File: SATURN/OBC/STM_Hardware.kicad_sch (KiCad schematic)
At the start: 6 parts, among them J1 SWD Pins, J2 USB_OTG, U1 USBLC6-4SC6

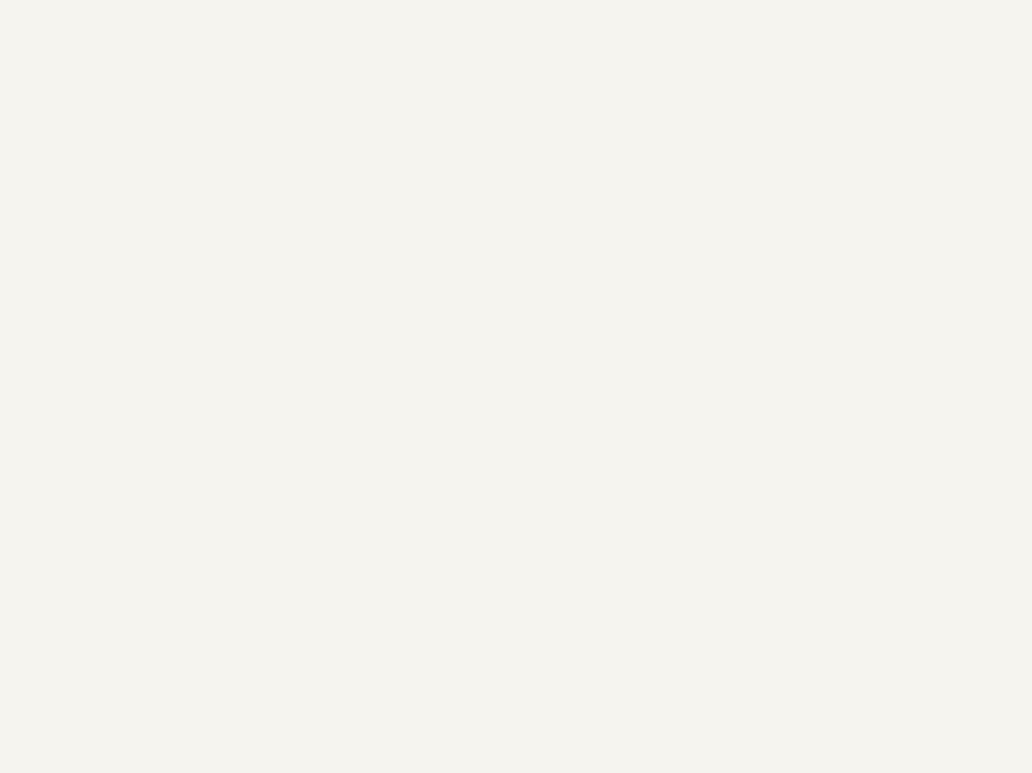
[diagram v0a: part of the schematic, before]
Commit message: Wired Up Watchdogs. Hopefully correctly.
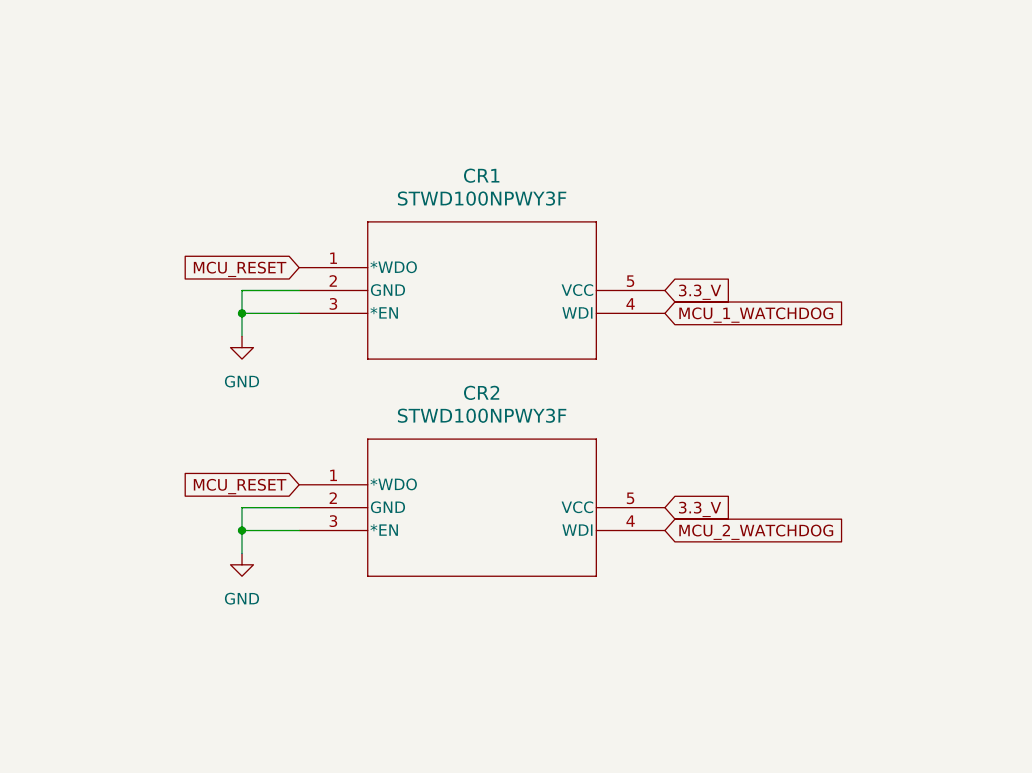
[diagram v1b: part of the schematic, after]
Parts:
- added CR1, CR2: STWD100NPWY3F, SOT23-5L_STM, symbol OBC-Components:STWD100NPWY3F
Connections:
- net GND: now also CR1.2 (GND), CR1.3 (*EN), CR2.2 (GND), CR2.3 (*EN)
- new net 3.3_V: CR1.5 (VCC), CR2.5 (VCC)
- new net MCU_1_WATCHDOG: CR1.4 (WDI)
- new net MCU_2_WATCHDOG: CR2.4 (WDI)
- new net MCU_RESET: CR1.1 (*WDO), CR2.1 (*WDO)

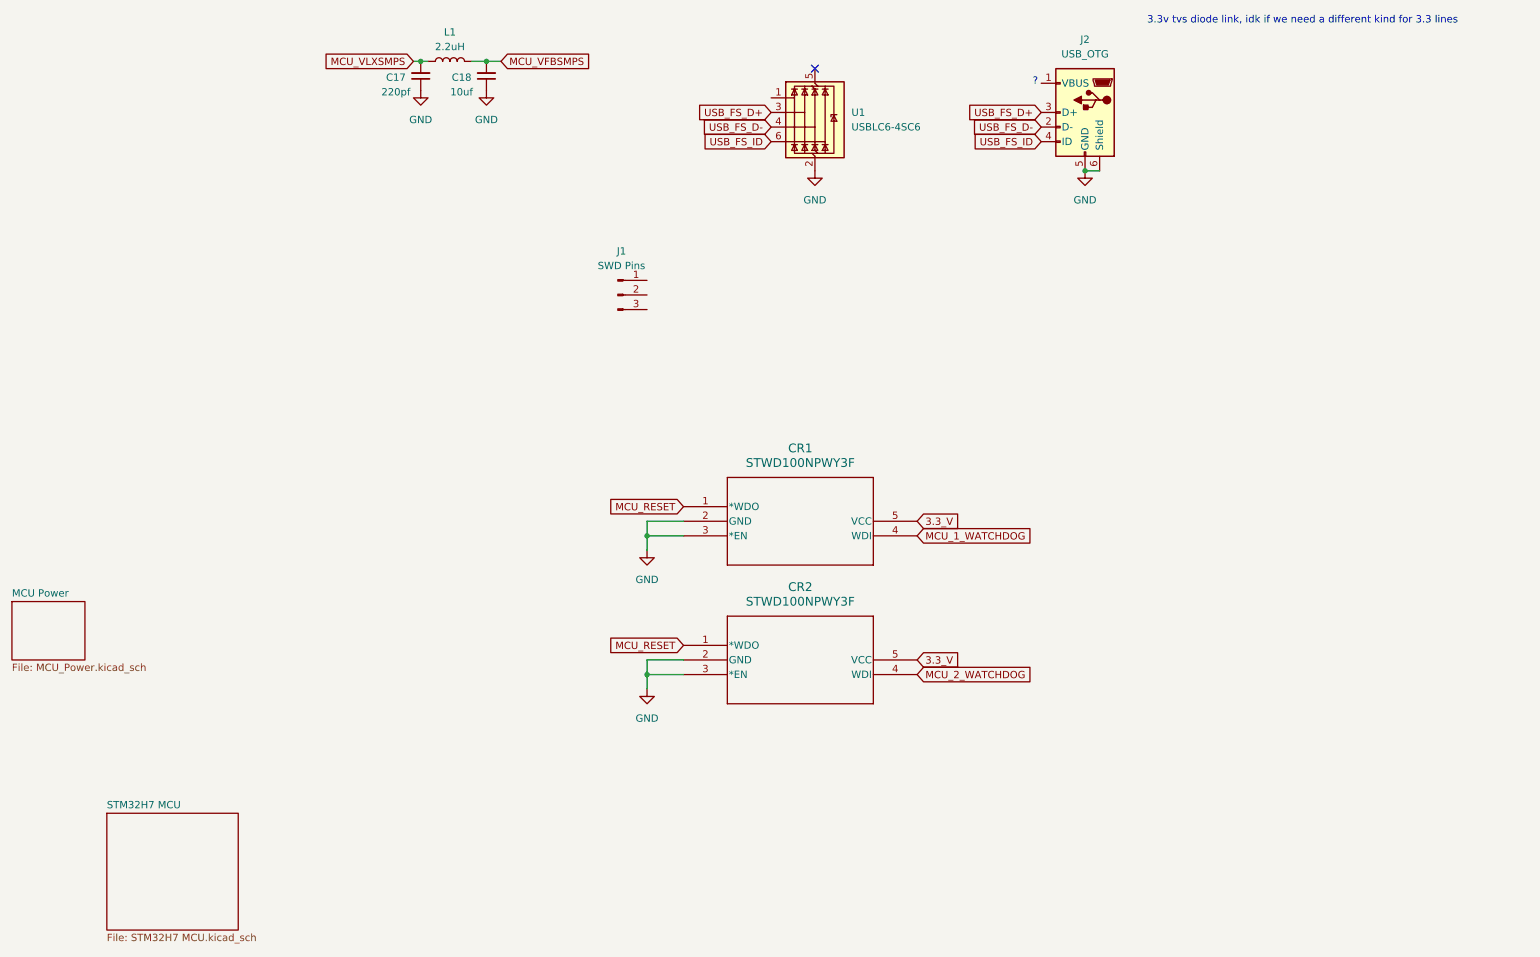
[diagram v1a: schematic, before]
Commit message: Some work on wiring up the RTC
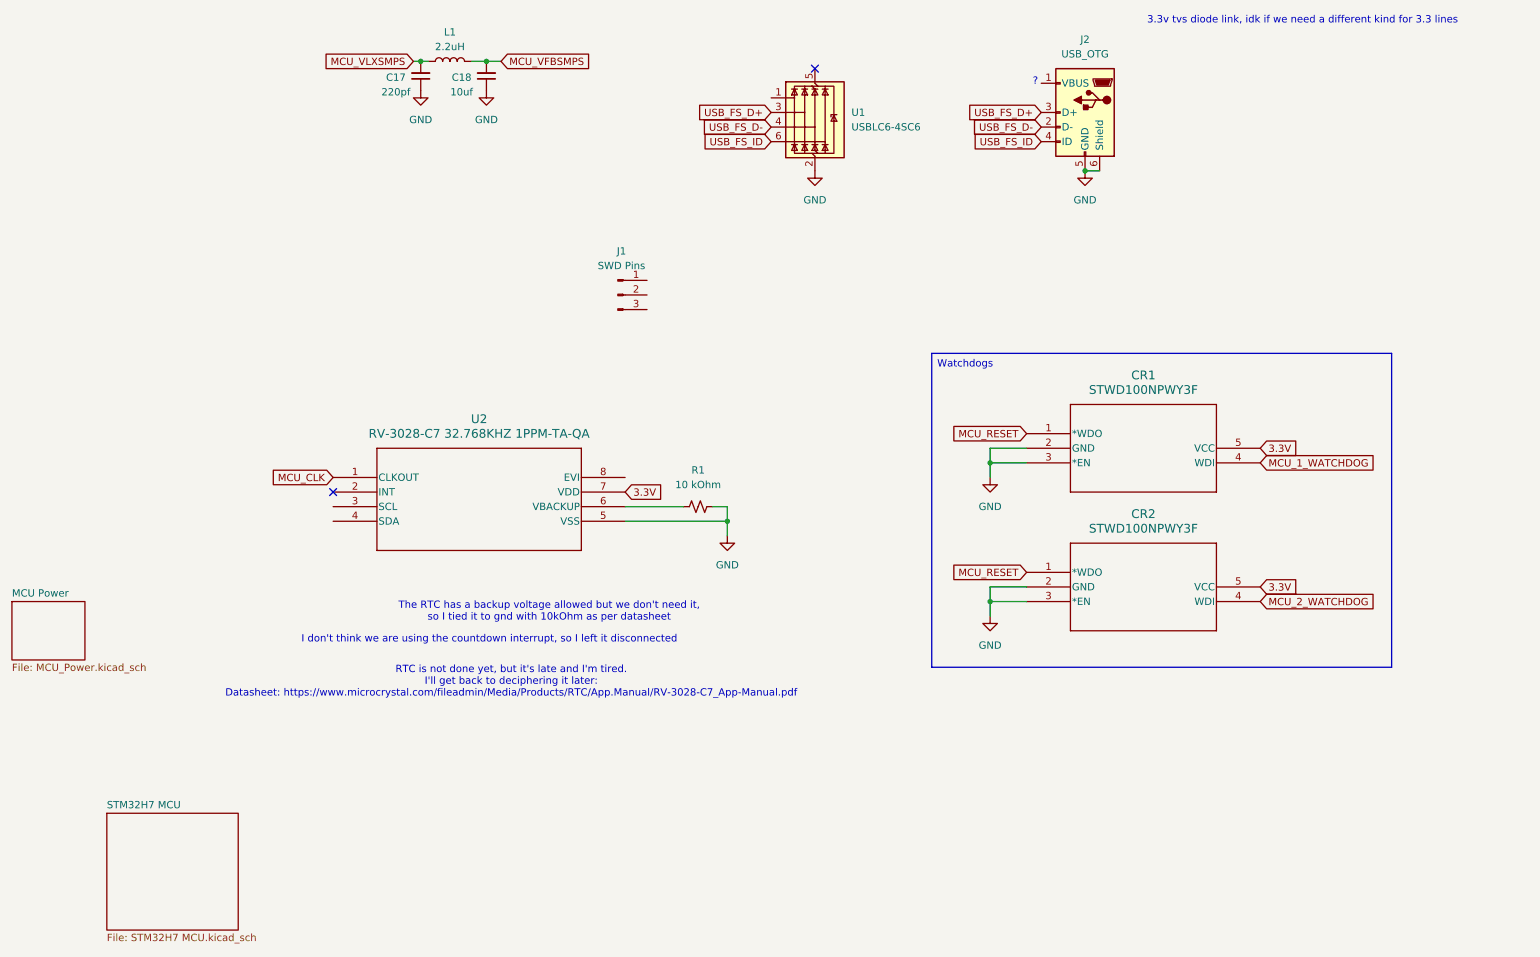
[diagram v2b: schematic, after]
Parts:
- added R1: 10 kOhm, symbol Device:R_Small_US
- added U2: RV-3028-C7 32.768KHZ 1PPM-TA-QA, RV-3028-C7_MCX, symbol OBC-Components:RV-3028-C7_32.768KHZ_1PPM-TA-QA
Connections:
- net GND: now also R1.2, U2.5 (VSS)
- net 3.3_V renamed 3.3V
- net 3.3V: now also U2.7 (VDD)
- new net: R1.1, U2.6 (VBACKUP)
- new net MCU_CLK: U2.1 (CLKOUT)
- no-connect marks 1 -> 2
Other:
- note added: "I don't think we are using the countdown interrupt, so I left it disconnected"
- note added: "RTC is not done yet, but it's late and I'm tired. I'll get back to deciphering it later: Datasheet: https://www.microcrystal.com/fileadmin/Media/Products/RTC/App.Manual/RV-3028-C7_App-Manual.pdf"
- note added: "The RTC has a backup voltage allowed but we don't need it, so I tied it to gnd with 10kOhm as per datasheet"
- moved on the sheet: CR1, CR2

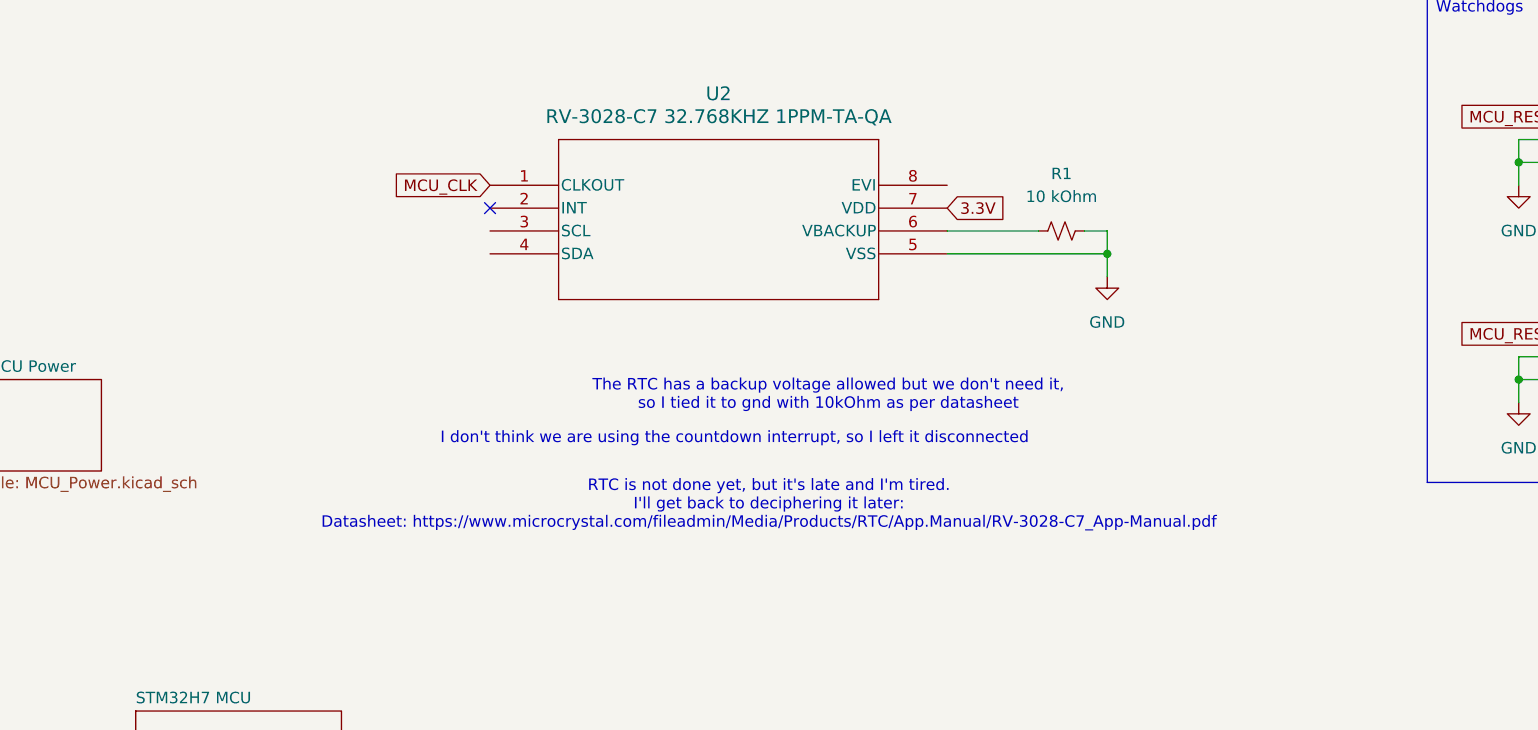
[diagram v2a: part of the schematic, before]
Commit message: Finished [TM] hooking up the RTC
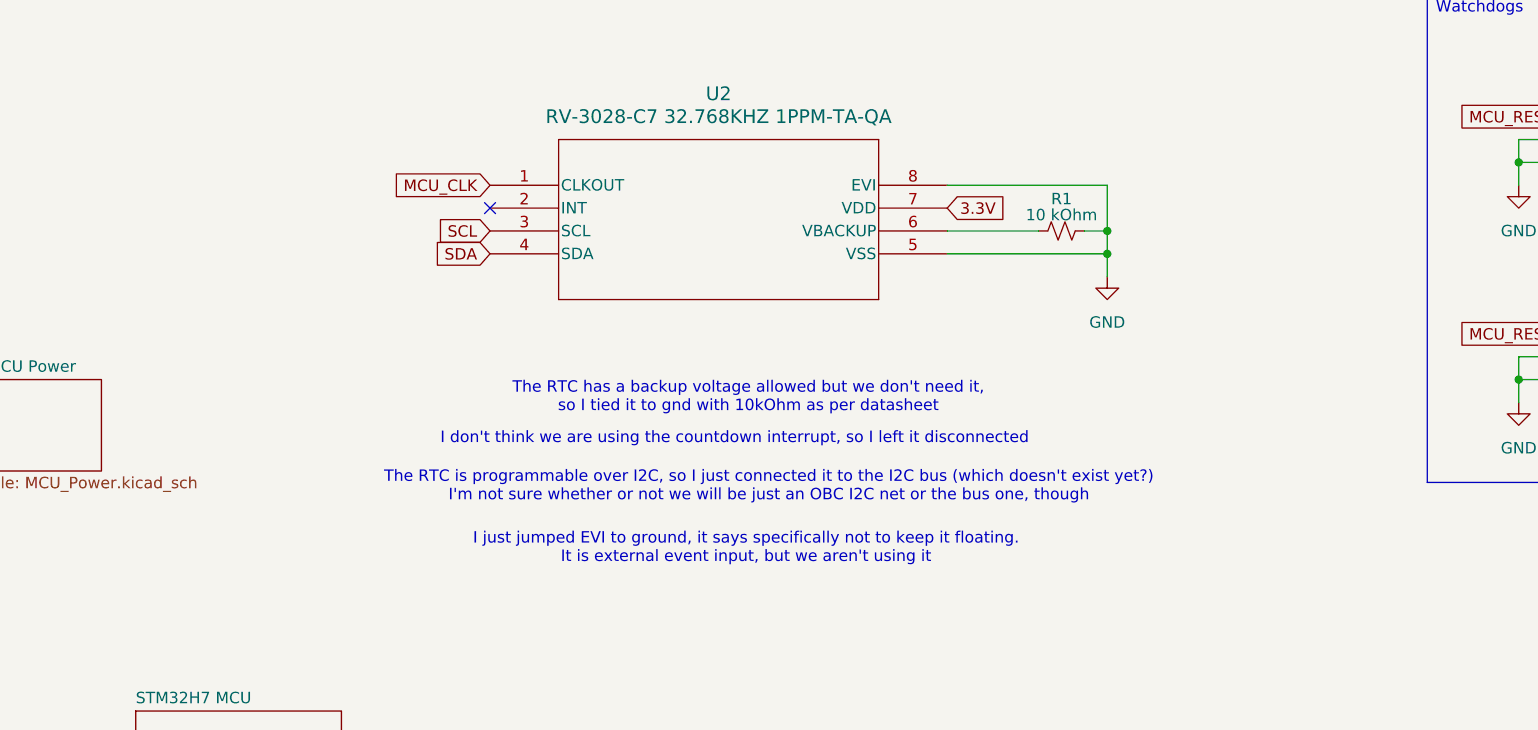
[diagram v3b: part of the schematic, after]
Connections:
- net GND: now also U2.8 (EVI)
- net SCL: now reaches U2.3 (SCL)
- net SDA: now reaches U2.4 (SDA)
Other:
- note added: "I just jumped EVI to ground, it says specifically not to keep it floating. It is external event input, but we aren't using it"
- note added: "The RTC is programmable over I2C, so I just connected it to the I2C bus (which doesn't exist yet?) I'm not sure whether or not we will be just an OBC I2C net or the bus one, though"
- note removed: "RTC is not done yet, but it's late and I'm tired. I'll get back to deciphering it later: Datasheet: https://www.microcrystal.com/fileadmin/Media/Products/RTC/App.Manual/RV-3028-C7_App-Manual.pdf"
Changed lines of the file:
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@@
 	(text "The RTC has a backup voltage allowed but we don't need it,\nso I tied it to gnd with 10kOhm as per datasheet\n"
 		(exclude_from_sim no)
-		(at 123.952 117.348 0)
-		(effects
-			(font
-				(size 1.27 1.27)
-			)
-		)
-	)
-	(text "RTC is not done yet, but it's late and I'm tired.\nI'll get back to deciphering it later:\nDatasheet: https://www.microcrystal.com/fileadmin/Media/Products/RTC/App.Manual/RV-3028-C7_App-Manual.pdf"
+		(at 115.062 117.602 0)
+		(effects
+			(font
+				(size 1.27 1.27)
+			)
+		)
+	)
+	(text "The RTC is programmable over I2C, so I just connected it to the I2C bus (which doesn't exist yet?)\nI'm not sure whether or not we will be just an OBC I2C net or the bus one, though"
 		(exclude_from_sim no)
-		(at 117.348 129.54 0)
+		(at 117.348 127.508 0)
+		(effects
+			(font
+				(size 1.27 1.27)
+			)
+		)
+	)
+	(text "I just jumped EVI to ground, it says specifically not to keep it floating.\nIt is external event input, but we aren't using it"
+		(exclude_from_sim no)
+		(at 114.808 134.366 0)
 		(effects
 			(font
@@
 		(color 0 0 0 0)
 	)
+	(junction
+		(at 154.94 99.06)
+		(diameter 0)
+		(color 0 0 0 0)
+	)
 	(no_connect
 		(at 170.18 22.86)
@@
 	(wire
 		(pts
+			(xy 137.16 93.98) (xy 154.94 93.98)
+		)
+		(stroke
+			(width 0)
+			(type default)
+		)
+	)
+	(wire
+		(pts
 			(xy 102.87 21.59) (xy 101.6 21.59)
 		)
@@
 	(wire
 		(pts
+			(xy 154.94 93.98) (xy 154.94 99.06)
+		)
+		(stroke
+			(width 0)
+			(type default)
+		)
+	)
+	(wire
+		(pts
 			(xy 154.94 99.06) (xy 154.94 101.6)
 		)
@@
 		)
 	)
+	(global_label "SDA"
+		(shape input)
+		(at 86.36 101.6 180)
+		(fields_autoplaced yes)
+		(effects
+			(font
+				(size 1.27 1.27)
+			)
+			(justify right)
+		)
+		(property "Intersheetrefs" "${INTERSHEET_REFS}"
+			(at 79.8067 101.6 0)
+			(hide yes)
+			(show_name no)
+			(do_not_autoplace no)
+			(effects
+				(font
+					(size 1.27 1.27)
+				)
+				(justify right)
+			)
+		)
+	)
 	(global_label "USB_FS_D+"
 		(shape input)
@@
 		(property "Intersheetrefs" "${INTERSHEET_REFS}"
 			(at 196.6467 35.56 0)
+			(hide yes)
+			(show_name no)
+			(do_not_autoplace no)
+			(effects
+				(font
+					(size 1.27 1.27)
+				)
+				(justify right)
+			)
+		)
+	)
+	(global_label "SCL"
+		(shape input)
+		(at 86.36 99.06 180)
+		(fields_autoplaced yes)
+		(effects
+			(font
+				(size 1.27 1.27)
+			)
+			(justify right)
+		)
+		(property "Intersheetrefs" "${INTERSHEET_REFS}"
+			(at 79.8672 99.06 0)
 			(hide yes)
 			(show_name no)
@@
 		(in_pos_files yes)
 		(dnp no)
-		(fields_autoplaced yes)
 		(property "Reference" "R1"
-			(at 149.86 92.71 90)
+			(at 149.86 95.504 90)
 			(show_name no)
 			(do_not_autoplace no)
@@
 		)
 		(property "Value" "10 kOhm"
-			(at 149.86 95.25 90)
-			(show_name no)
-			(do_not_autoplace no)
+			(at 149.86 97.282 90)
+			(show_name no)
+			(do_not_autoplace no)
